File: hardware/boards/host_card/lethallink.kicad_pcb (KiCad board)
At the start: 6 copper layers, 121.2 x 98.4 mm, 205 parts, among them J1 PCIe-x4, J2 USB3_Micro_B_Amphenol, J3 Conn_02x05_Odd_Even, J4 Conn_02x04_Odd_Even, J5 Conn_02x04_Odd_Even, J6 SODIMM_260, Q1 Q_NMOS_GSD, Q2 Q_NMOS_GSD, Q3 Q_NMOS_GSD, Q4 Q_NMOS_GSD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

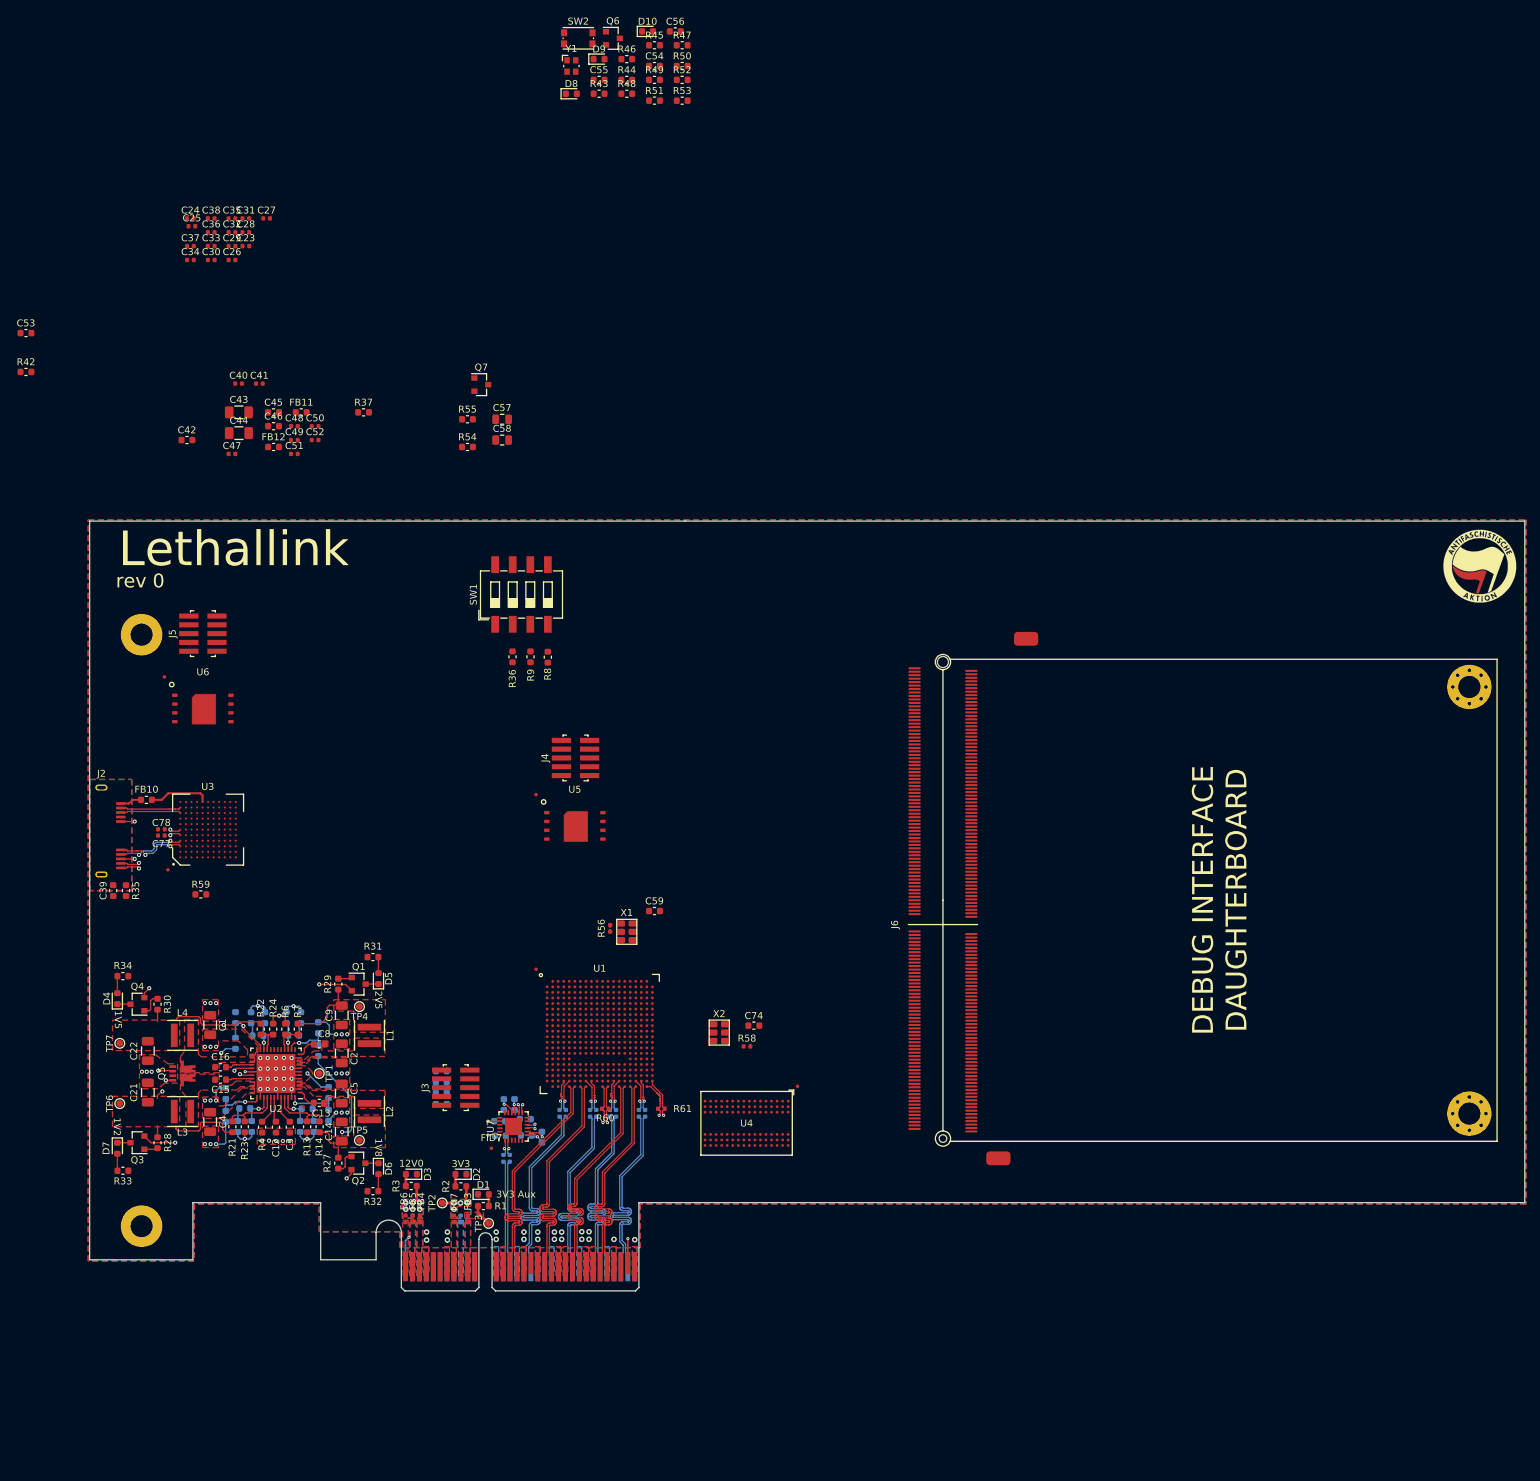
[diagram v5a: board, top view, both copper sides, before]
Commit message: Re-routed the USB side of things after adding the ESD diodes for the USB SS lines, still need to add the diode for the normal D+/D- pair
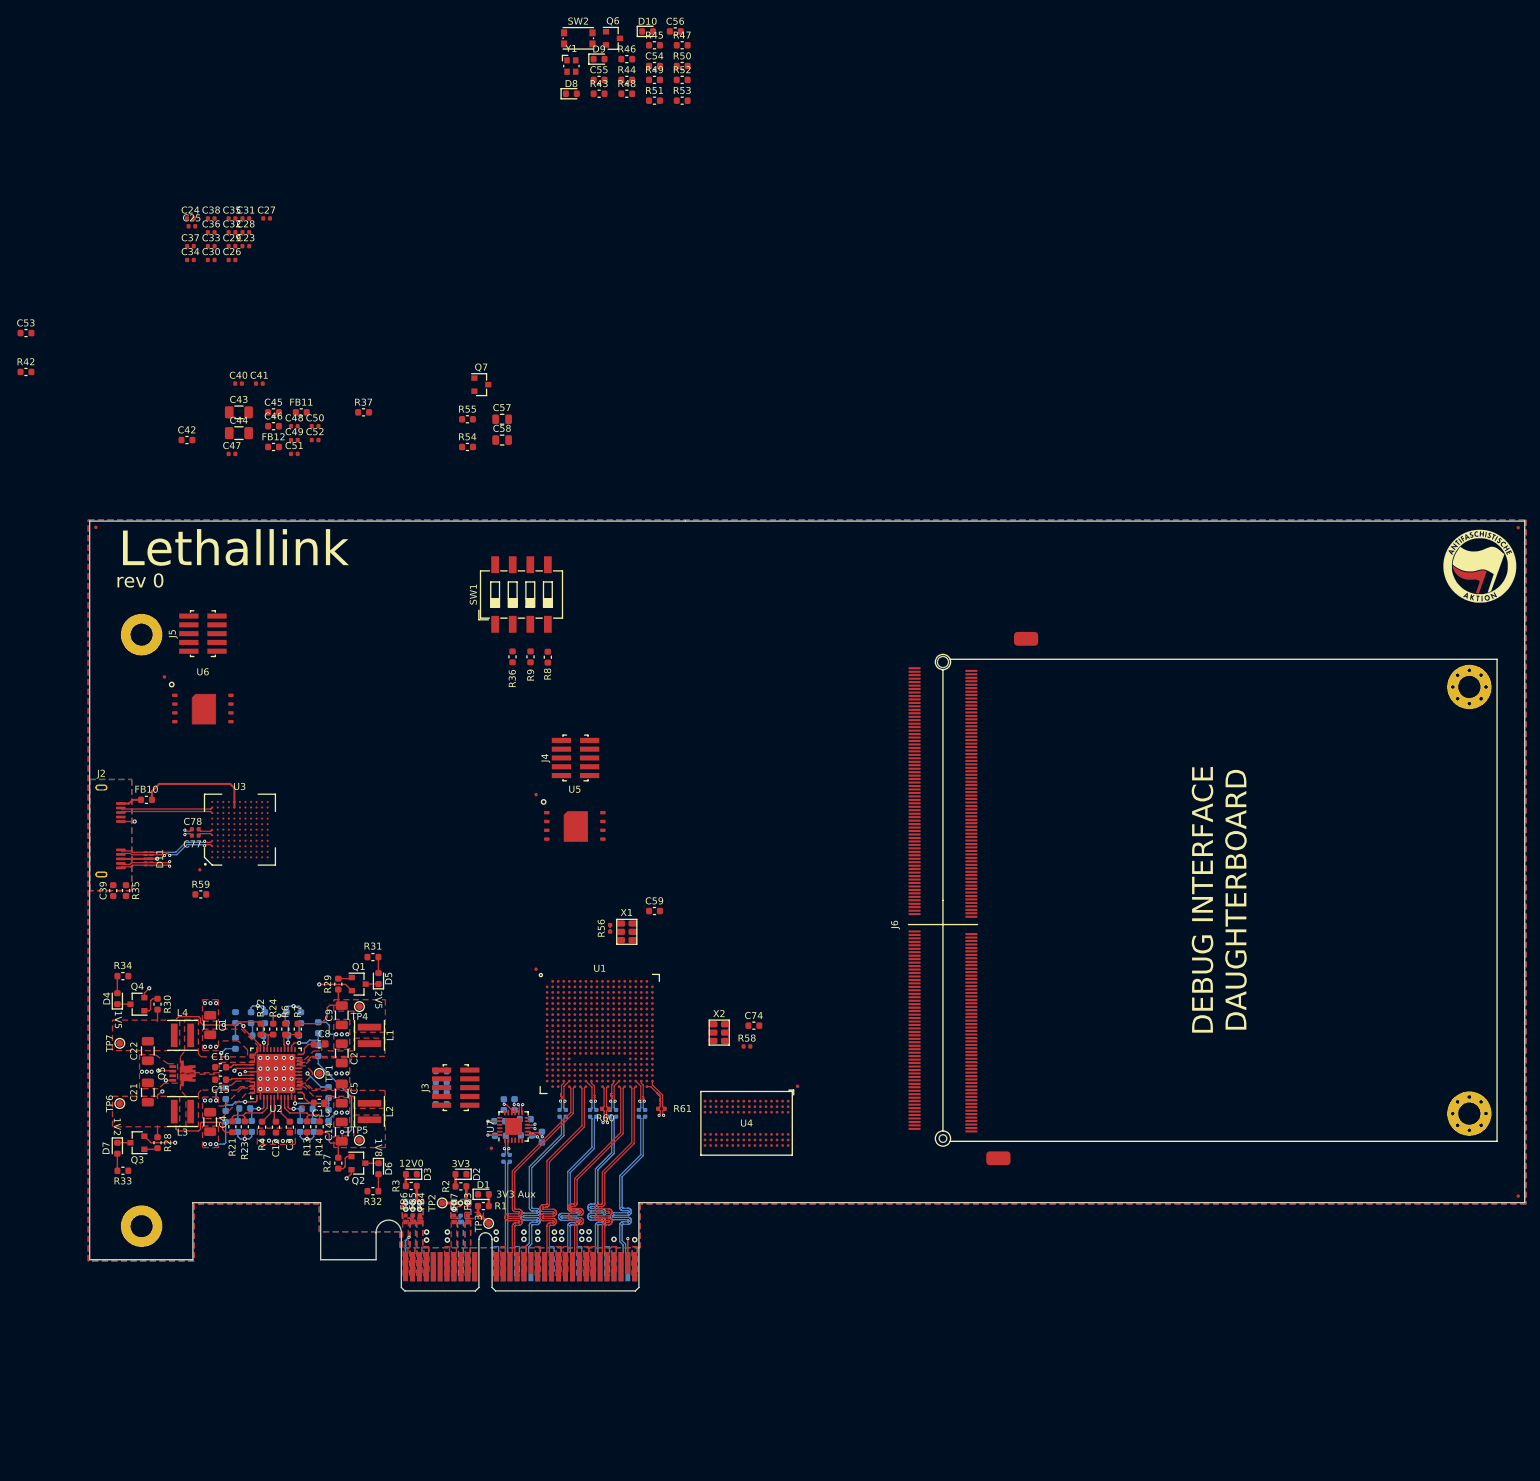
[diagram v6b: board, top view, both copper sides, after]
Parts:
- added D11: RClamp3324P, lethalbit:RClamp3324P, F.Cu at (25.9, 64.5)
- added FID10: Fiducial, Fiducial:Fiducial_0.5mm_Mask1mm, F.Cu at (18.4, 16.6)
- added FID8: Fiducial, Fiducial:Fiducial_0.5mm_Mask1mm, F.Cu at (223.7, 113.2)
- added FID9: Fiducial, Fiducial:Fiducial_0.5mm_Mask1mm, F.Cu at (223.7, 16.6)
- moved C77 4.90 mm to (32.7, 61.1), turned to 180 degrees
- moved C78 4.90 mm to (32.7, 60.2), turned to 180 degrees
- moved FID1 4.60 mm to (33.4, 66.0)
- moved U3 4.60 mm to (39.1, 60.2)
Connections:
- net Net-(C77-Pad1) renamed /USB3 Interface/PSSTX+
- net Net-(C78-Pad1) renamed /USB3 Interface/PSSTX-
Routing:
- net Net-(FB10-Pad1): track 8.78 -> 16.6 mm
- net /USB3 Interface/D-: track 8.90 -> 13.5 mm
- net /USB3 Interface/D+: track 8.90 -> 13.5 mm
- net /USB3 Interface/SSRX+: track 10.2 -> 14.5 mm
- net /USB3 Interface/SSRX-: track 10.2 -> 14.5 mm
- net GND: track 60.5 -> 63.8 mm
- net /USB3 Interface/PSSTX+: track 0.00 -> 2.17 mm
- net /USB3 Interface/PSSTX-: track 0.00 -> 2.17 mm
- net /USB3 Interface/SSTX+: track 13.1 -> 14.1 mm
- net /USB3 Interface/SSTX-: track 13.1 -> 14.1 mm

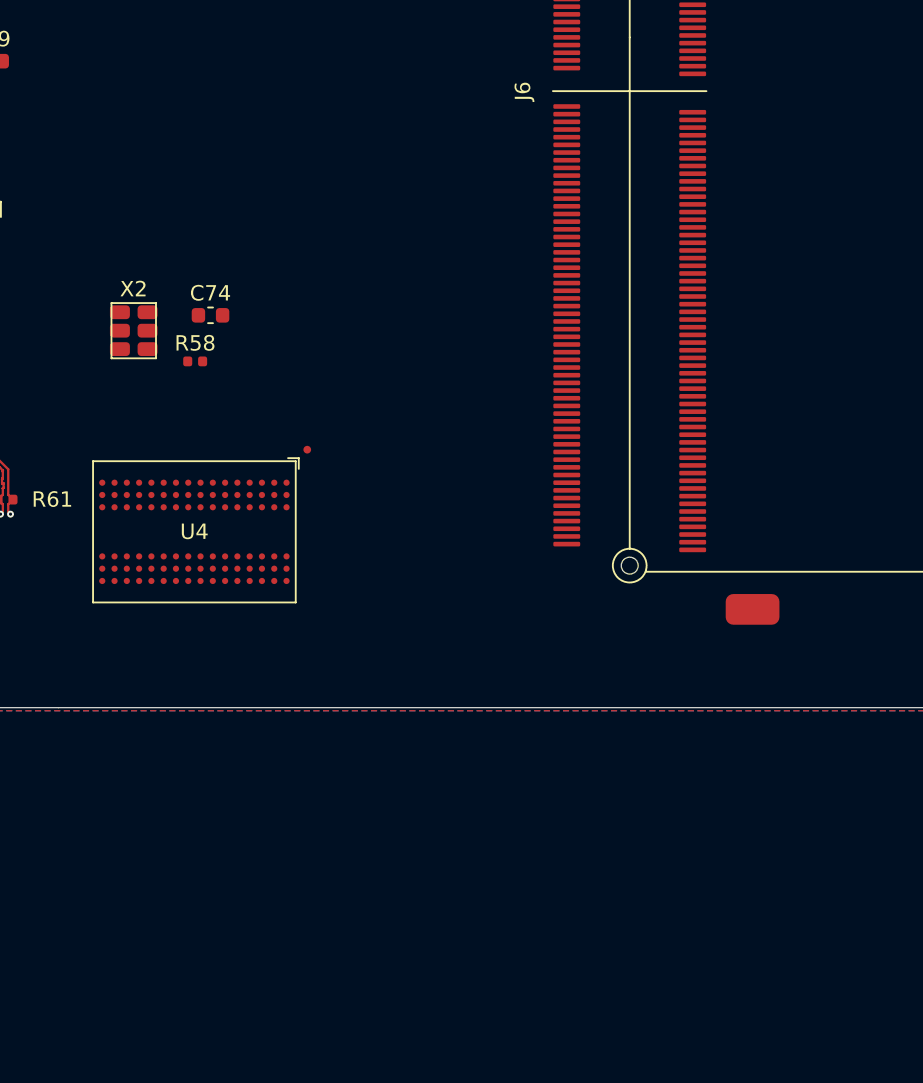
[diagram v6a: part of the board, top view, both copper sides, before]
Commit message: Added another DDR3 module to expand cache to 8GiB
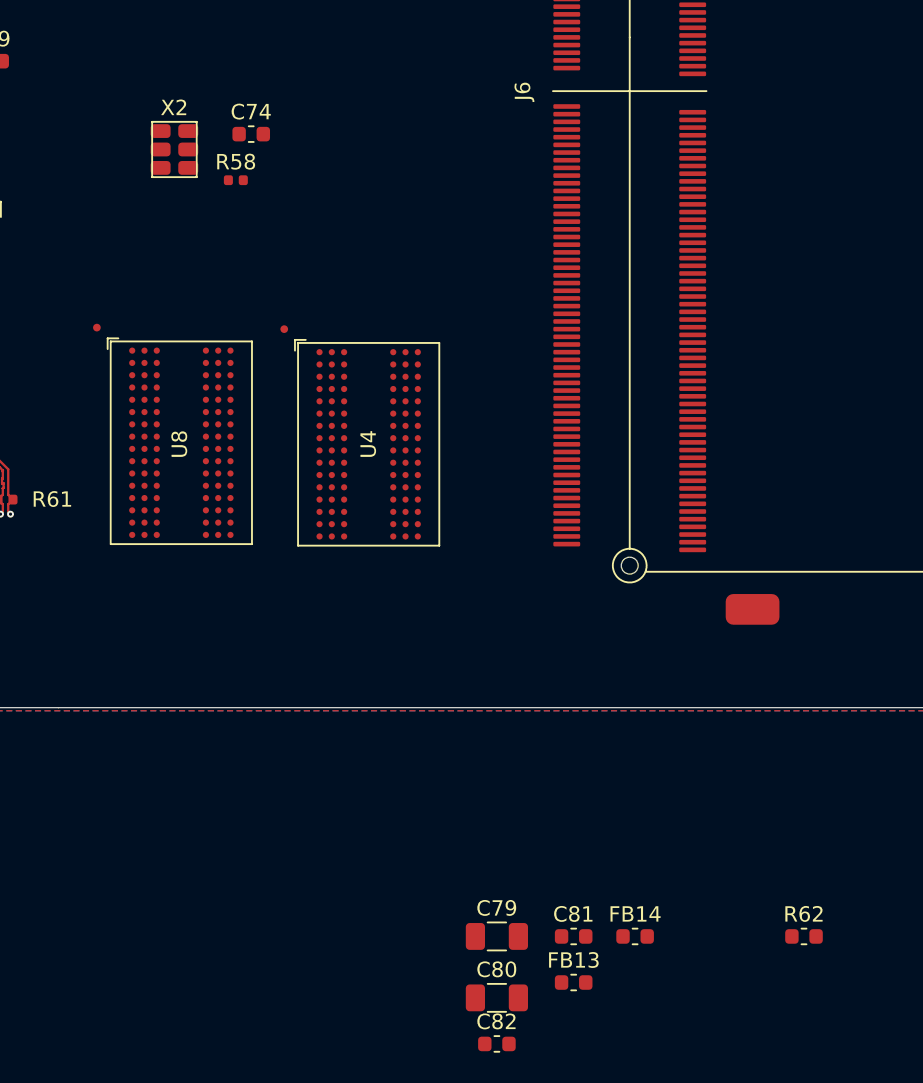
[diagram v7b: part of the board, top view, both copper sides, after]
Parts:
- added C79: 22uF, Capacitor_SMD:C_1206_3216Metric, F.Cu at (132.0, 129.0)
- added C80: 22uF, Capacitor_SMD:C_1206_3216Metric, F.Cu at (132.0, 133.0)
- added C81: 1uF, Capacitor_SMD:C_0603_1608Metric, F.Cu at (137.0, 129.0)
- added C82: 1uF, Capacitor_SMD:C_0603_1608Metric, F.Cu at (132.0, 136.0)
- added FB13: 220 @ 100Mhz, Resistor_SMD:R_0603_1608Metric, F.Cu at (137.0, 132.0)
- added FB14: 220 @ 100Mhz, Resistor_SMD:R_0603_1608Metric, F.Cu at (141.0, 129.0)
- added FID11: Fiducial, Fiducial:Fiducial_0.5mm_Mask1mm, F.Cu at (106.0, 89.3)
- added R62: 240, Resistor_SMD:R_0603_1608Metric, F.Cu at (152.0, 129.0)
- added U8: IS43TR16256B-125KBL, Package_BGA:BGA-96_9.0x13.0mm_Layout2x3x16_P0.8mm, F.Cu at (111.5, 96.8)
- moved U4 12.7 mm to (123.7, 97.0), turned to 0 degrees
- moved C74 12.1 mm to (116.0, 76.8)
- moved R58 12.1 mm to (115.0, 79.8)
- moved X2 12.1 mm to (111.0, 77.8)
- moved FID5 7.99 mm to (118.2, 89.5), turned to 270 degrees

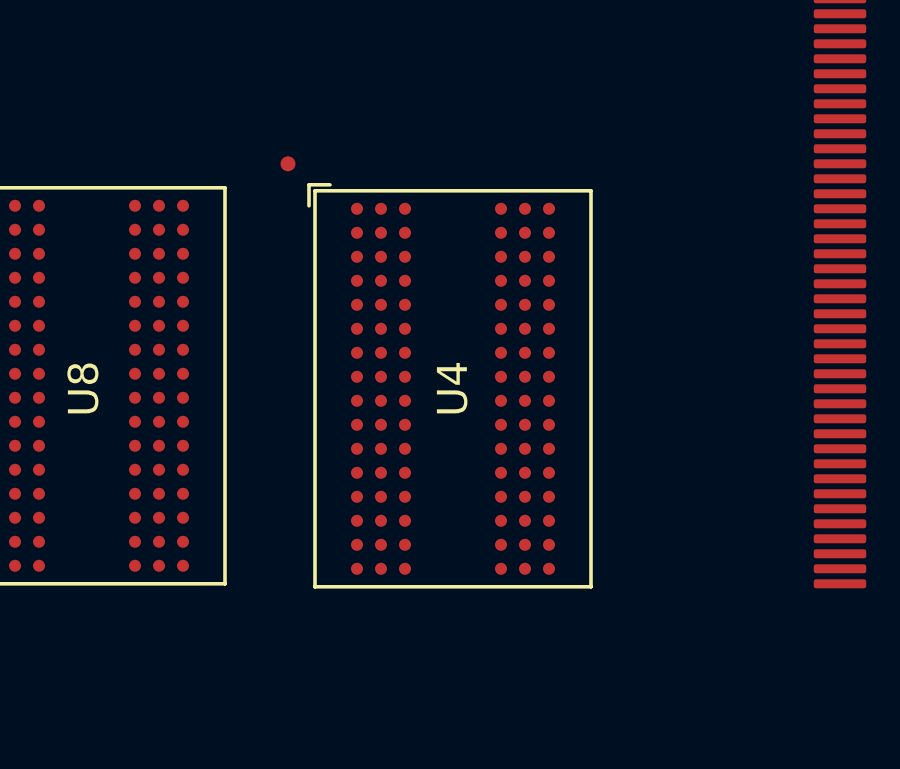
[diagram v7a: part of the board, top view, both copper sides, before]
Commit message: Fixed the pour keepout for the DDR3 modules
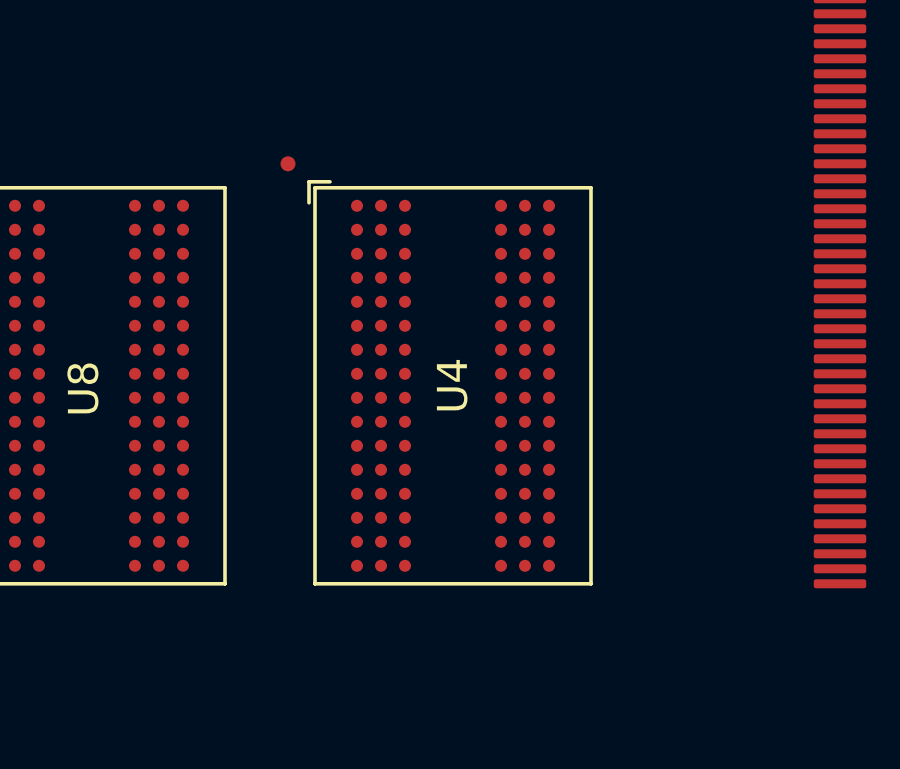
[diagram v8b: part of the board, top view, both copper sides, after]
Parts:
- moved U4 0.10 mm to (123.7, 96.8)
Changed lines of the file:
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@@
   )
   (module Package_BGA:BGA-96_9.0x13.0mm_Layout2x3x16_P0.8mm (layer F.Cu)
-    (at 123.65 96.95)
+    (at 123.65 96.85)
     (descr "BGA-96, http://www.mouser.com/ds/2/198/43-46TR16640B-81280BL-706483.pdf")
     (tags BGA-96)
@@
     )
   )
-  (zone (net 0) (net_name "") (layer F.Cu) (hatch edge 0.508)
-    (connect_pads yes (clearance 0.1))
-    (min_thickness 0.2)
-    (keepout (tracks allowed) (vias allowed) (copperpour not_allowed))
-    (fill (arc_segments 32) (thermal_gap 0.2) (thermal_bridge_width 0.4))
-    (polygon
-      (pts
-        (xy 122.7 103.35) (xy 122.45 103.55) (xy 120.05 103.55) (xy 119.85 103.35) (xy 119.85 90.55)
-        (xy 120.05 90.35) (xy 122.45 90.35) (xy 122.7 90.55)
-      )
-    )
-  )
-  (zone (net 0) (net_name "") (layer F.Cu) (hatch edge 0.508)
-    (connect_pads yes (clearance 0.1))
-    (min_thickness 0.2)
-    (keepout (tracks allowed) (vias allowed) (copperpour not_allowed))
-    (fill (arc_segments 32) (thermal_gap 0.2) (thermal_bridge_width 0.4))
-    (polygon
-      (pts
-        (xy 127.5 103.35) (xy 127.25 103.55) (xy 124.85 103.55) (xy 124.65 103.35) (xy 124.65 90.55)
-        (xy 124.85 90.35) (xy 127.25 90.35) (xy 127.5 90.55)
-      )
-    )
-  )
   (zone (net 710) (net_name "Net-(FB1-Pad2)") (layer F.Cu) (hatch edge 0.508)
     (priority 2)
@@
     (polygon
       (pts
-        (xy 115.25 103.2) (xy 115 103.4) (xy 112.6 103.4) (xy 112.4 103.2) (xy 112.4 90.4)
-        (xy 112.6 90.2) (xy 115 90.2) (xy 115.25 90.4)
+        (xy 110.45 103.25) (xy 110.2 103.45) (xy 107.85 103.45) (xy 107.65 103.25) (xy 107.65 90.45)
+        (xy 107.85 90.25) (xy 110.2 90.25) (xy 110.45 90.45)
+      )
+    )
+  )
+  (zone (net 0) (net_name "") (layer F.Cu) (hatch edge 0.508)
+    (connect_pads yes (clearance 0.1))
+    (min_thickness 0.2)
+    (keepout (tracks allowed) (vias allowed) (copperpour not_allowed))
+    (fill (arc_segments 32) (thermal_gap 0.2) (thermal_bridge_width 0.4))
+    (polygon
+      (pts
+        (xy 115.25 103.25) (xy 115 103.45) (xy 112.65 103.45) (xy 112.45 103.25) (xy 112.45 90.45)
+        (xy 112.65 90.25) (xy 115 90.25) (xy 115.25 90.45)
+      )
+    )
+  )
+  (zone (net 0) (net_name "") (layer F.Cu) (hatch edge 0.508)
+    (connect_pads yes (clearance 0.1))
+    (min_thickness 0.2)
+    (keepout (tracks allowed) (vias allowed) (copperpour not_allowed))
+    (fill (arc_segments 32) (thermal_gap 0.2) (thermal_bridge_width 0.4))
+    (polygon
+      (pts
+        (xy 122.65 103.25) (xy 122.4 103.45) (xy 120.05 103.45) (xy 119.85 103.25) (xy 119.85 90.45)
+        (xy 120.05 90.25) (xy 122.4 90.25) (xy 122.65 90.45)
       )
     )
@@
     (polygon
       (pts
-        (xy 110.45 103.25) (xy 110.2 103.45) (xy 107.8 103.45) (xy 107.6 103.25) (xy 107.6 90.45)
-        (xy 107.8 90.25) (xy 110.2 90.25) (xy 110.45 90.45)
+        (xy 127.45 103.25) (xy 127.2 103.45) (xy 124.85 103.45) (xy 124.65 103.25) (xy 124.65 90.45)
+        (xy 124.85 90.25) (xy 127.2 90.25) (xy 127.45 90.45)
       )
     )
